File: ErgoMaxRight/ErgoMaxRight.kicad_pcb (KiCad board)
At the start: 2 copper layers, 182.8 x 169.2 mm, 98 parts, among them J1 PJ-320A, K1 KEYSW, K10 KEYSW, K11 KEYSW, K12 KEYSW, K13 KEYSW, K14 KEYSW, K15 KEYSW, K16 KEYSW, K17 KEYSW, K18 KEYSW, K19 KEYSW, K2 KEYSW, K20 KEYSW, K21 KEYSW, K22 KEYSW, K23 KEYSW, K24 KEYSW, K25 KEYSW, K26 KEYSW, K27 KEYSW, K28 KEYSW, K29 KEYSW, K3 KEYSW, K30 KEYSW, K31 KEYSW, K32 KEYSW, K33 KEYSW, K34 KEYSW, K35 KEYSW, K36 KEYSW, K37 KEYSW, K38 KEYSW, K39 KEYSW, K4 KEYSW, K40 KEYSW, K41 KEYSW, K42 KEYSW, K43 KEYSW, K44 KEYSW, K5 KEYSW, K6 KEYSW, K7 KEYSW, K8 KEYSW, K9 KEYSW, U1 ProMicro

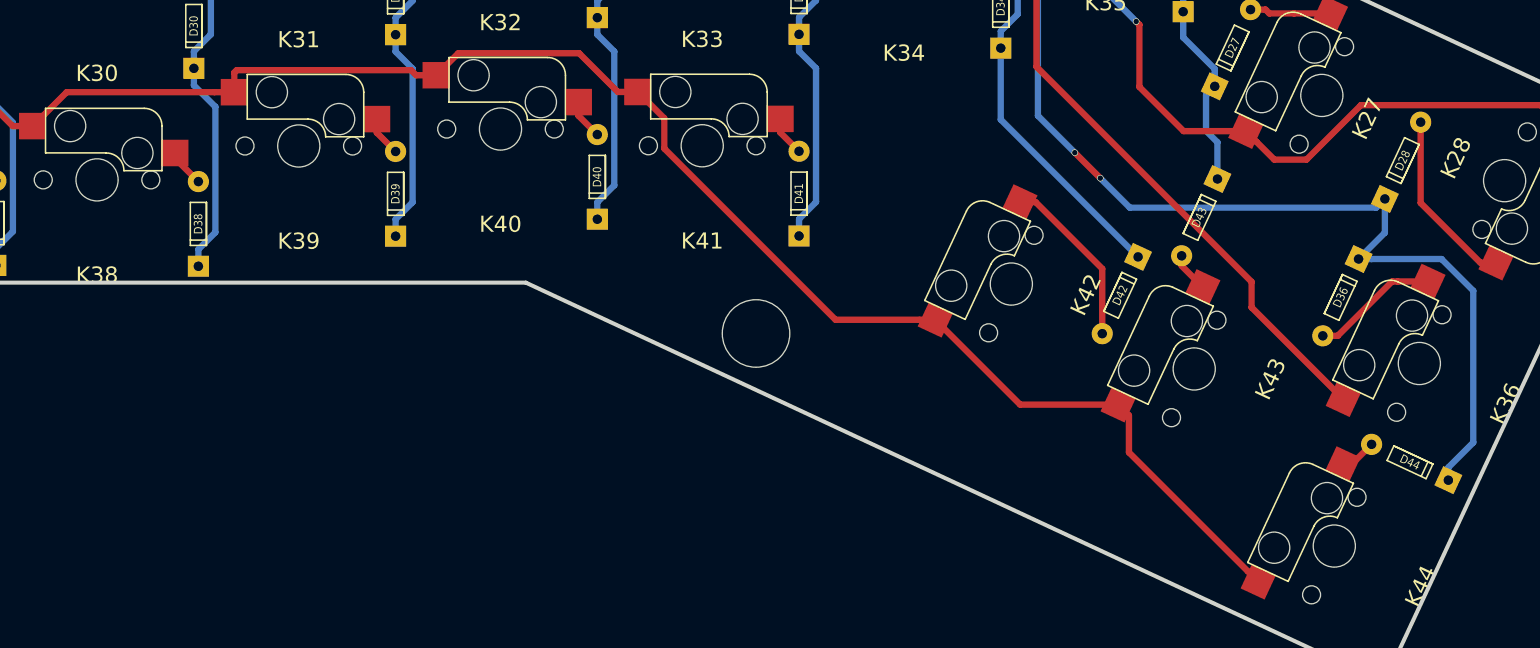
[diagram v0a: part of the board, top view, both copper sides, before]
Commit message: add a 2u stab for thumb key - WIP
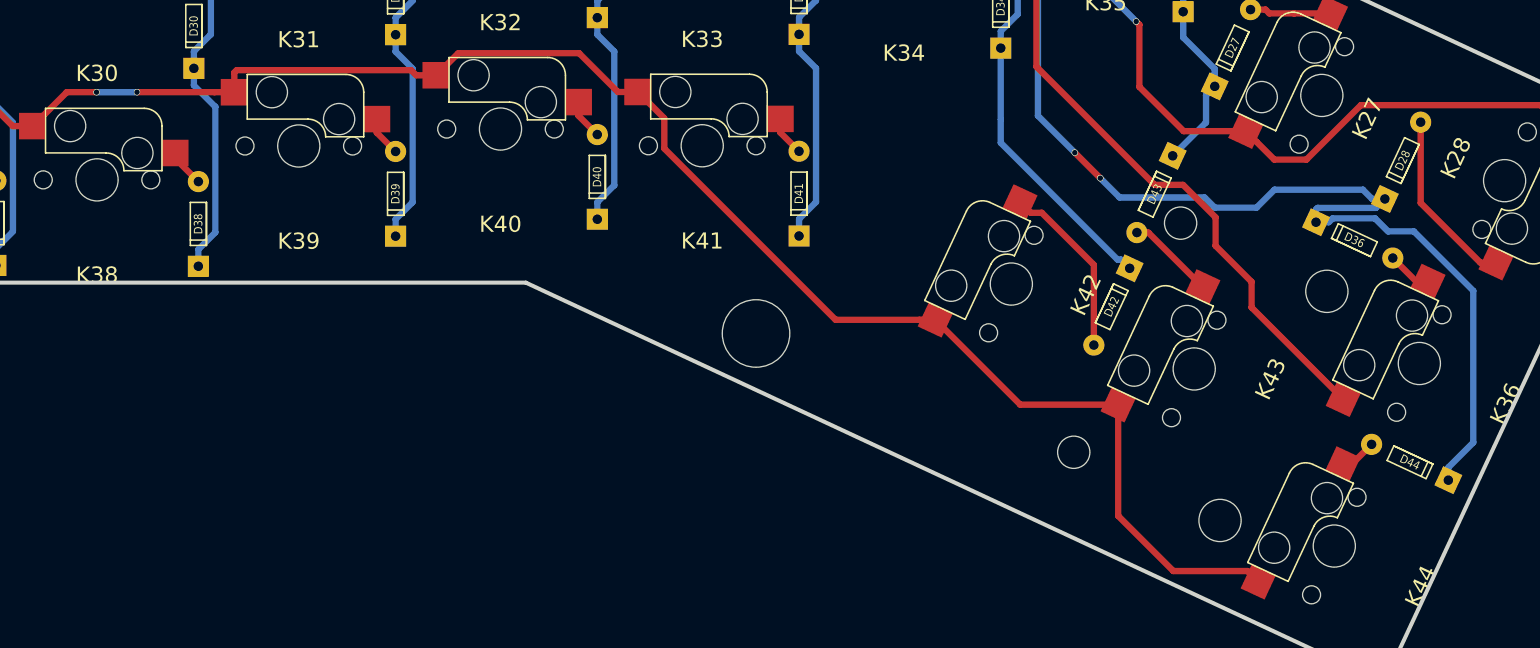
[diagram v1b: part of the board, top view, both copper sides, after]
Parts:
- added ST72: Stabilizer, keyboard_parts:Mx_Stab_200, F.Cu at (252.2, 176.7)
- moved D36 5.56 mm to (267.4, 164.6), turned to 155 degrees
- moved D43 4.76 mm to (248.5, 160.2)
- moved D42 1.34 mm to (244.4, 170.8)
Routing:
- net /Col7: track 276.8 -> 284.7 mm
- net Net-(D36-Pad2): track 12.1 -> 4.23 mm
- net Net-(D43-Pad2): track 3.77 -> 8.35 mm
- net /Row5: track 279.7 -> 283.8 mm, vias 0 -> 2
- net /Row4: track 287.9 -> 289.5 mm
- net /Col6: track 247.7 -> 246.4 mm
- net /Col5: track 224.2 -> 225.2 mm
- net Net-(D42-Pad2): track 16.5 -> 17.0 mm

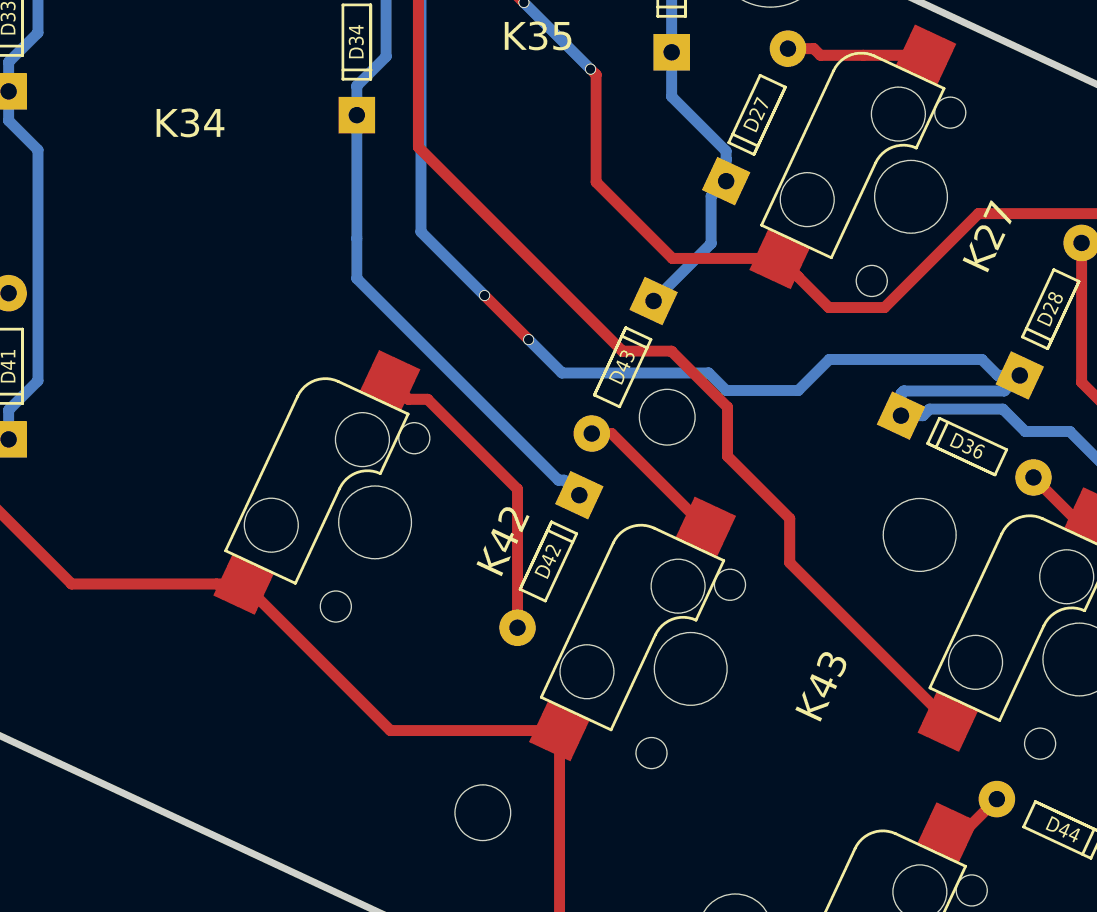
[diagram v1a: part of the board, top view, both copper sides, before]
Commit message: add second stab to thumb key
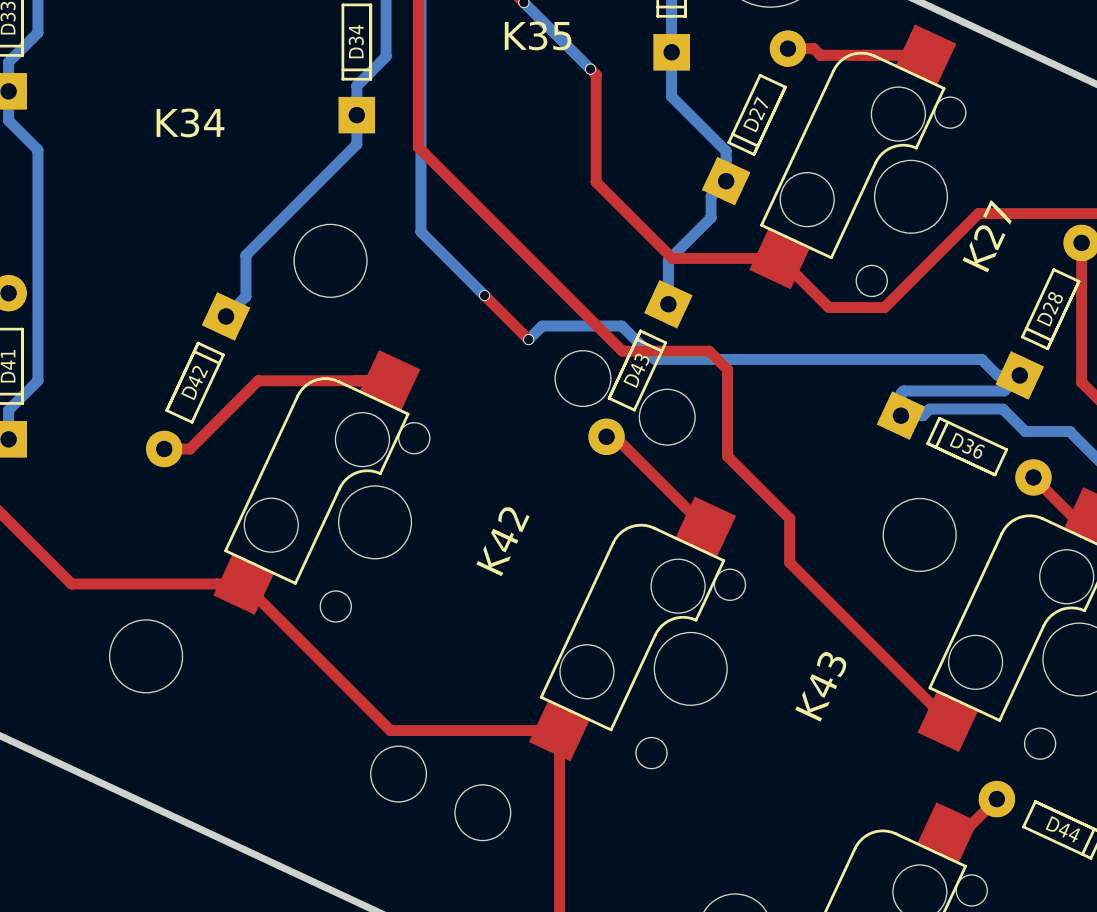
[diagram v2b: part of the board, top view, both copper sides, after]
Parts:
- added ST72: Stabilizer, keyboard_parts:Mx_Stab_200, F.Cu at (235.0, 168.7)
- moved D42 21.7 mm to (225.1, 161.1)
- moved D43 0.83 mm to (249.3, 160.4)
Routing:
- net /Col5: track 225.2 -> 213.1 mm
- net Net-(D42-Pad2): track 17.0 -> 15.8 mm
- net /Row4: track 289.5 -> 290.7 mm
- net Net-(D43-Pad2): track 8.35 -> 7.47 mm
- net /Col7: track 284.7 -> 283.9 mm

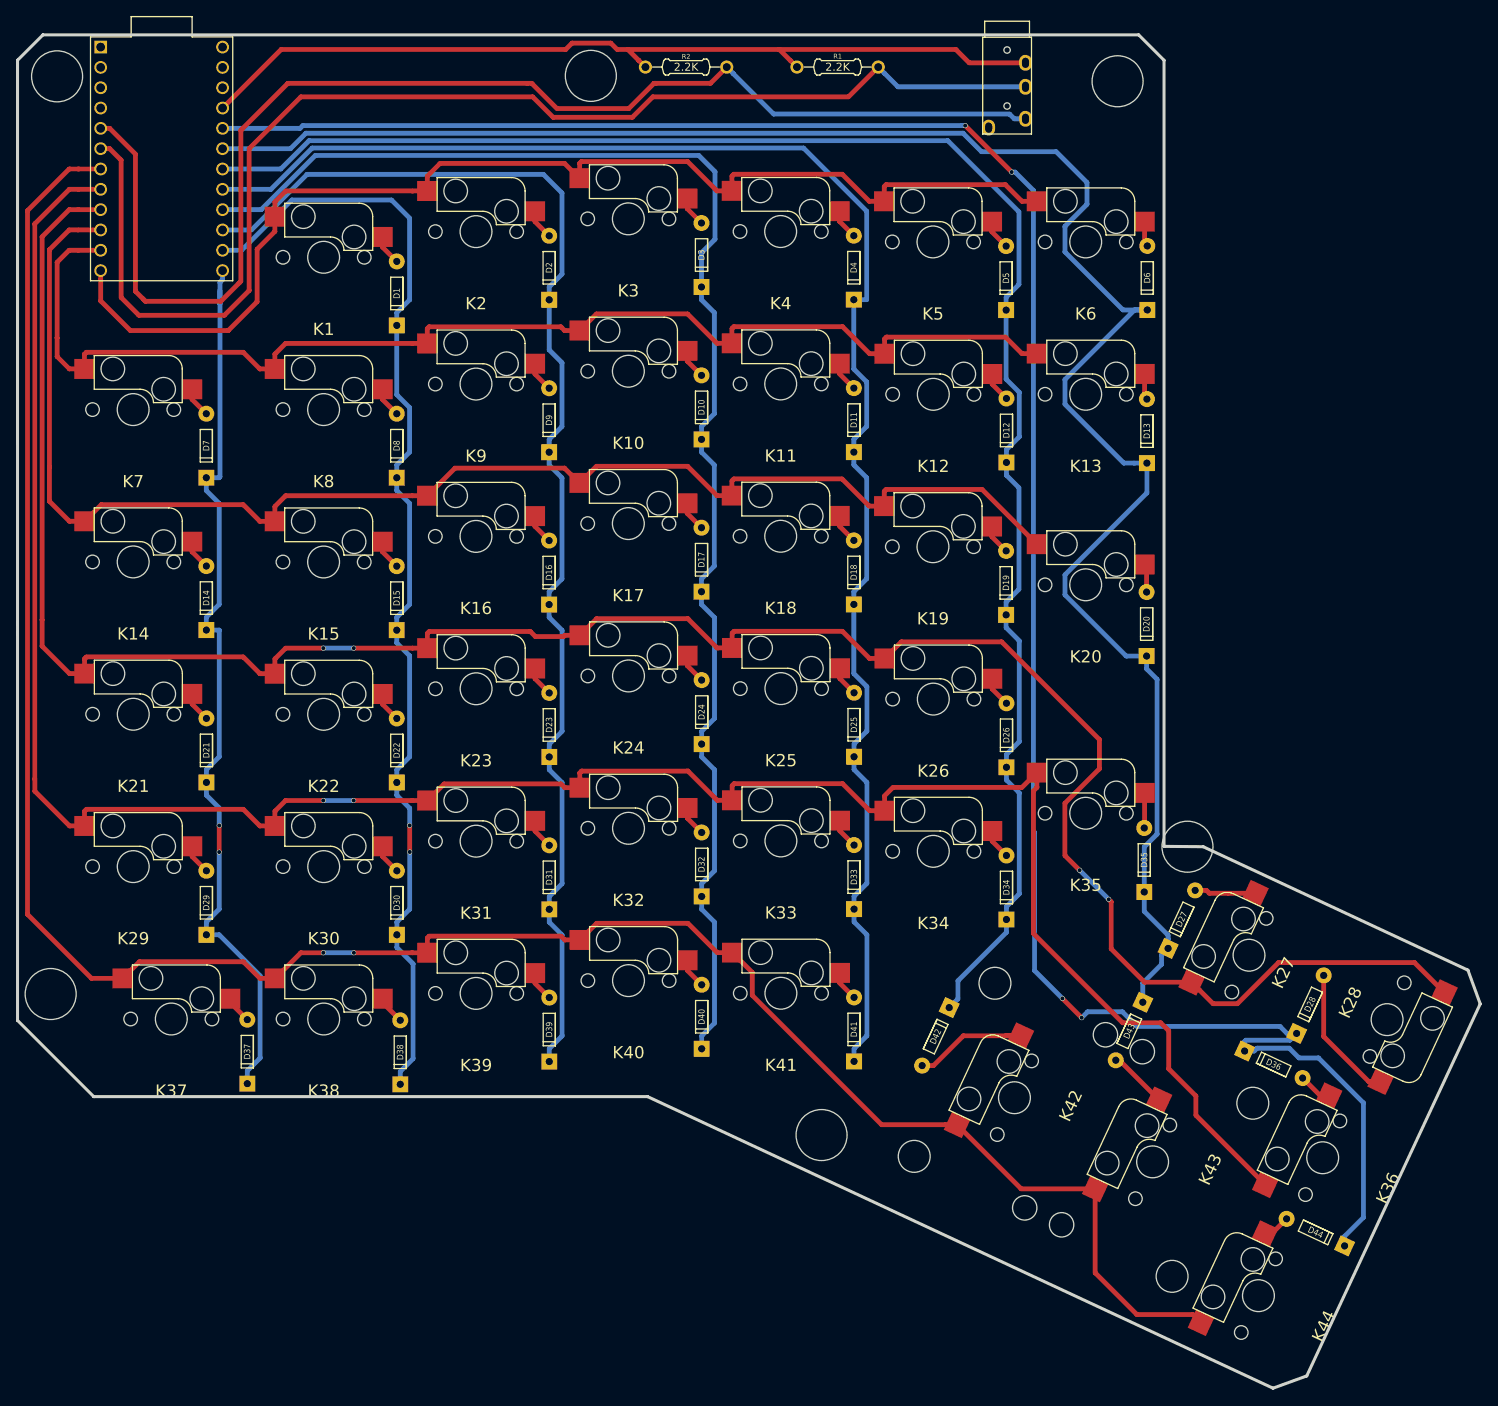
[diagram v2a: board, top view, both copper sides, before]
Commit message: modify library for MX Kailh sockets; add mounting holes in schema for PCB
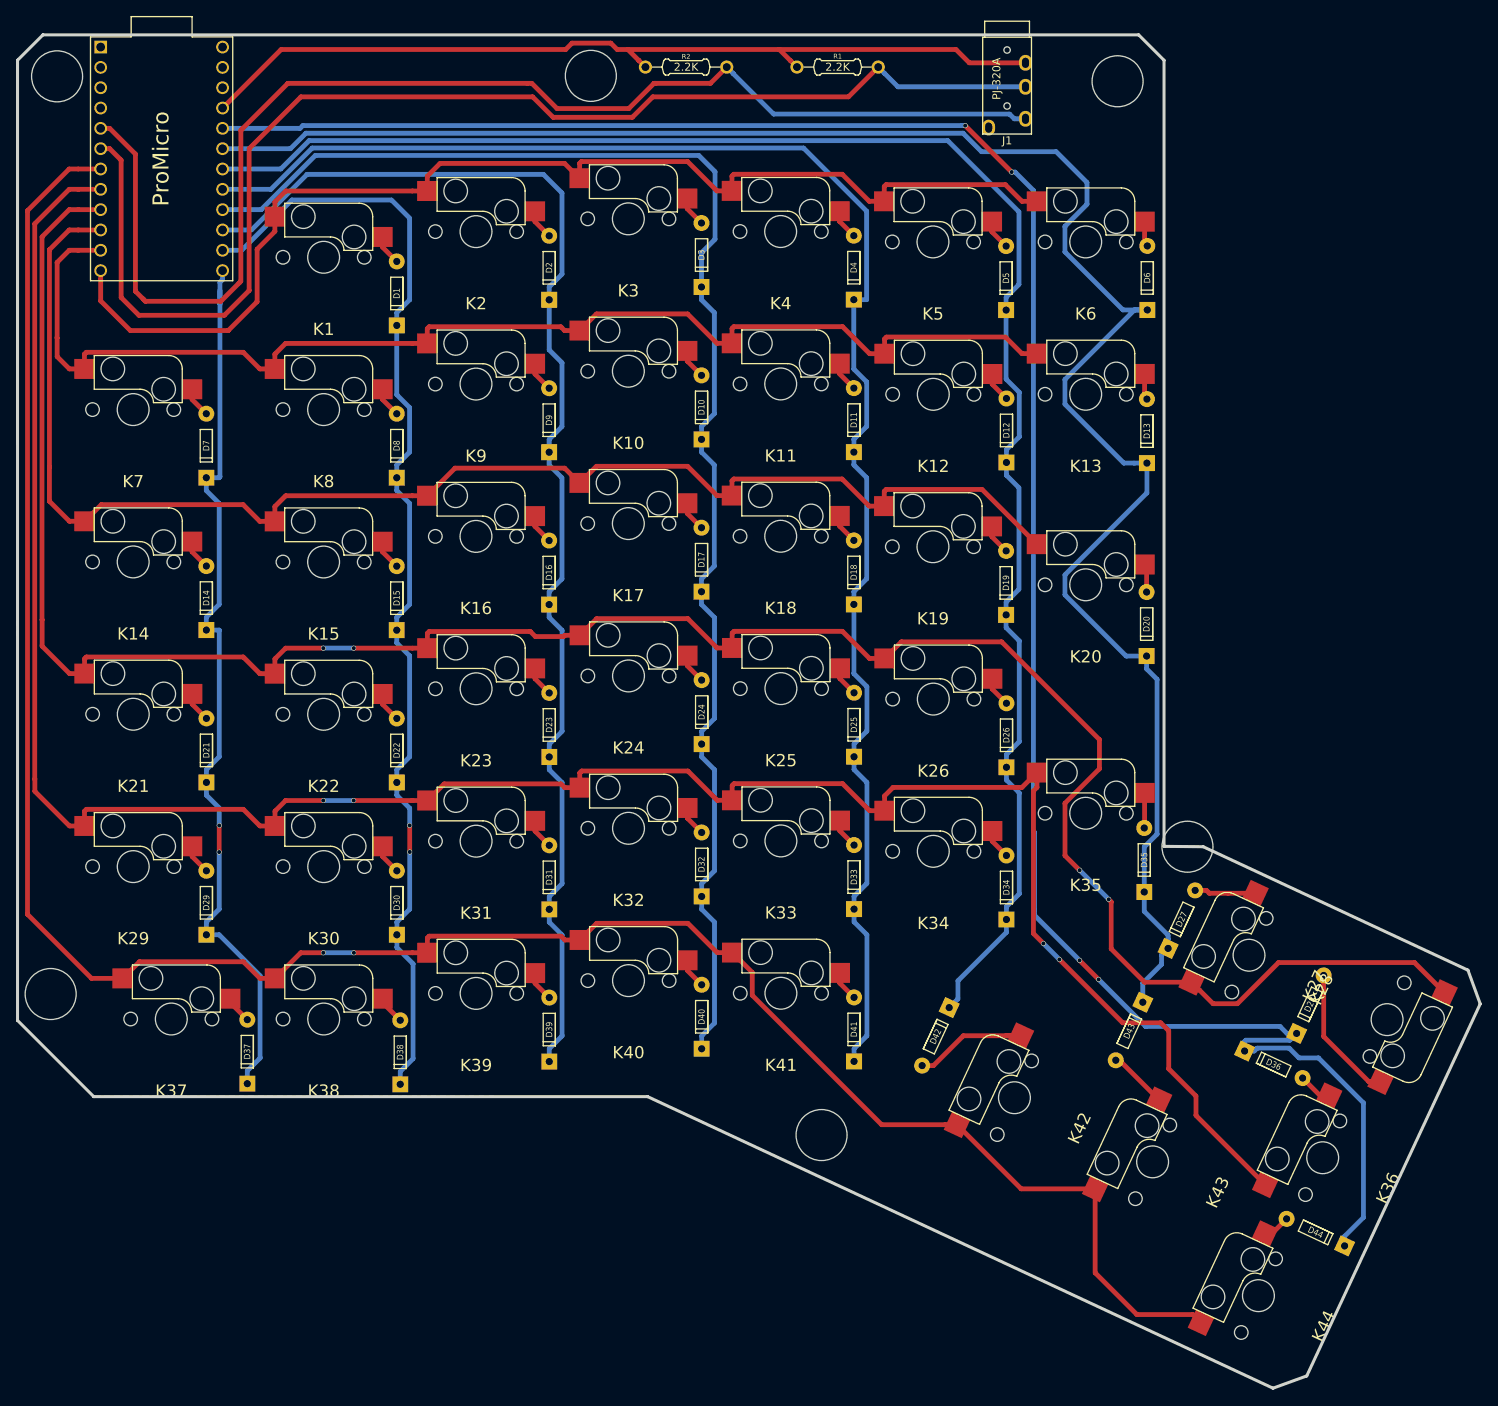
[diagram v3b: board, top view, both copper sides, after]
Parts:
- removed ST72 (x2): Stabilizer, keyboard_parts:Mx_Stab_200
- H1, H2, H3, H4, H5, H6: renamed from REF**; value MountingHole_6mm -> MountingHole
- K1, K10, K11, K12, K13, K14, K15, K16, K17, K18, K19, K2, K20, K21, K22, K23, K24, K25, K26, K27, K28, K29, K3, K30, K31, K32, K33, K34, K35, K36, K37, K38, K39, K4, K40, K41, K42, K43, K44, K5, K6, K7, K8, K9: footprint keyboard_parts:Kailh_MX_Socket -> Kailh_MX_socket:Kailh_MX_Socket
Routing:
- net /Col7: track 283.9 -> 279.2 mm
- net /Row4: vias 2 -> 4
